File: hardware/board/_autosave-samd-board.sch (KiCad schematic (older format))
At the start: 26 parts, among them J1 USB_B_Mini, J2 Conn_ARM_JTAG_SWD_10, J3 Conn_01x16_Male, J4 Conn_01x16_Male, SW1 SW_Push, U1 AZ1117-3.3, U2 ATSAMD21E17D-A, Y1 8MHz

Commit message: increase pin count from 28 to 32, complete routing
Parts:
- C2: value 10u 10V -> 10u 16V
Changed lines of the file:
@@
 P 5700 1750
 F 0 "C2" H 5550 1800 50  0000 R CNN
-F 1 "10u 10V" H 5550 1700 50  0000 R CNN
+F 1 "10u 16V" H 5550 1700 50  0000 R CNN
 F 2 "Capacitor_Tantalum_SMD:CP_EIA-3216-18_Kemet-A_Pad1.58x1.35mm_HandSolder" H 5738 1600 50  0001 C CNN
 F 3 "~" H 5700 1750 50  0001 C CNN

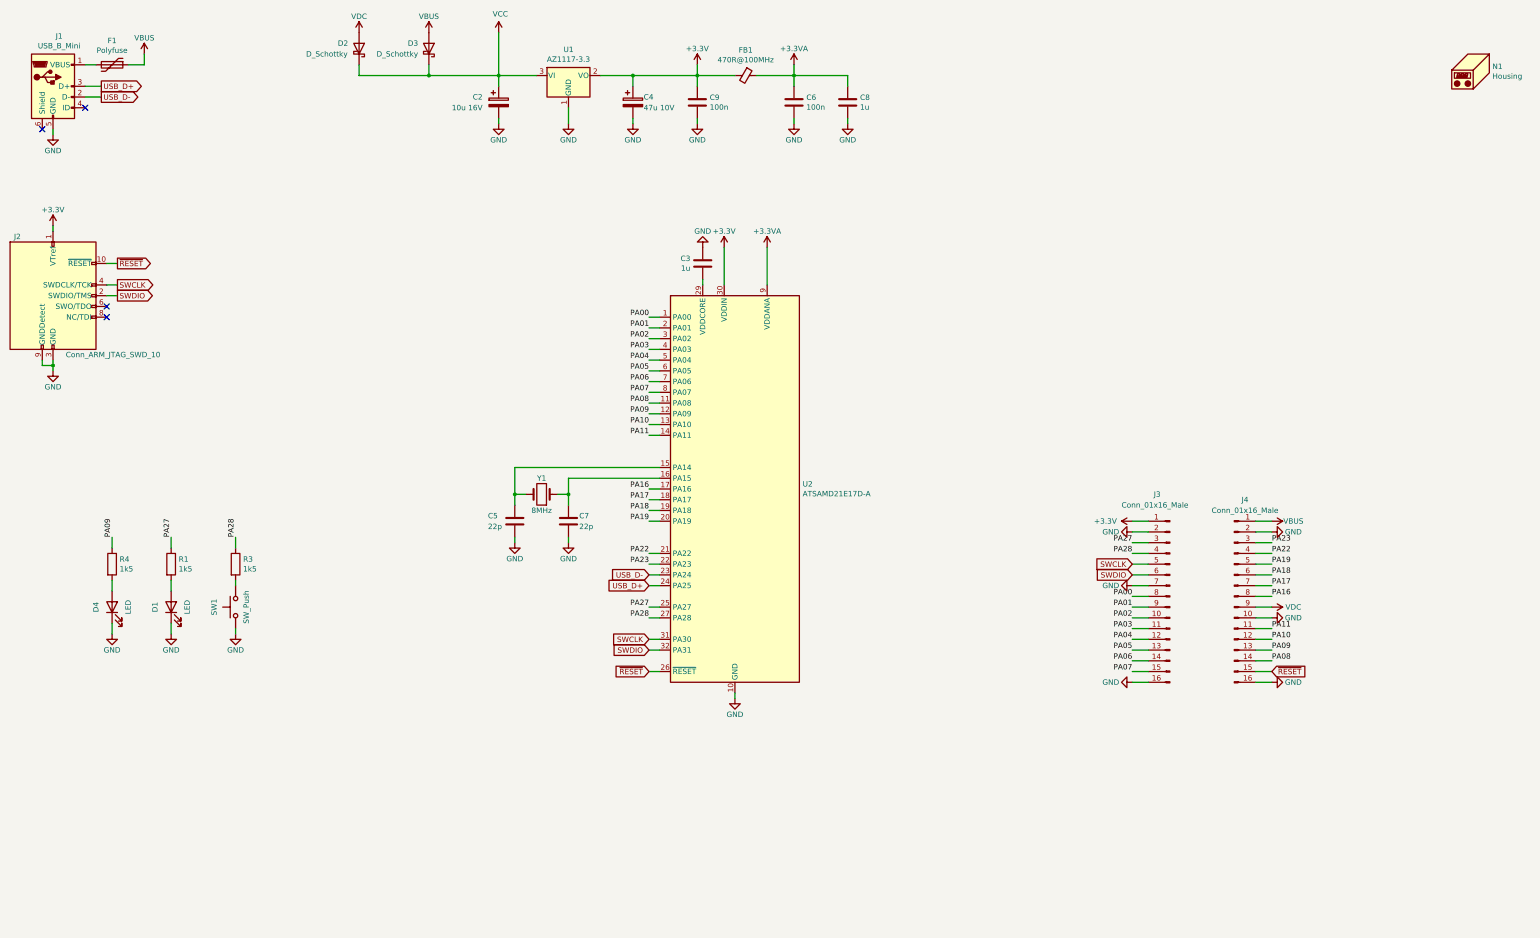
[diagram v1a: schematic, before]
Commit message: complete component silkscreen placement
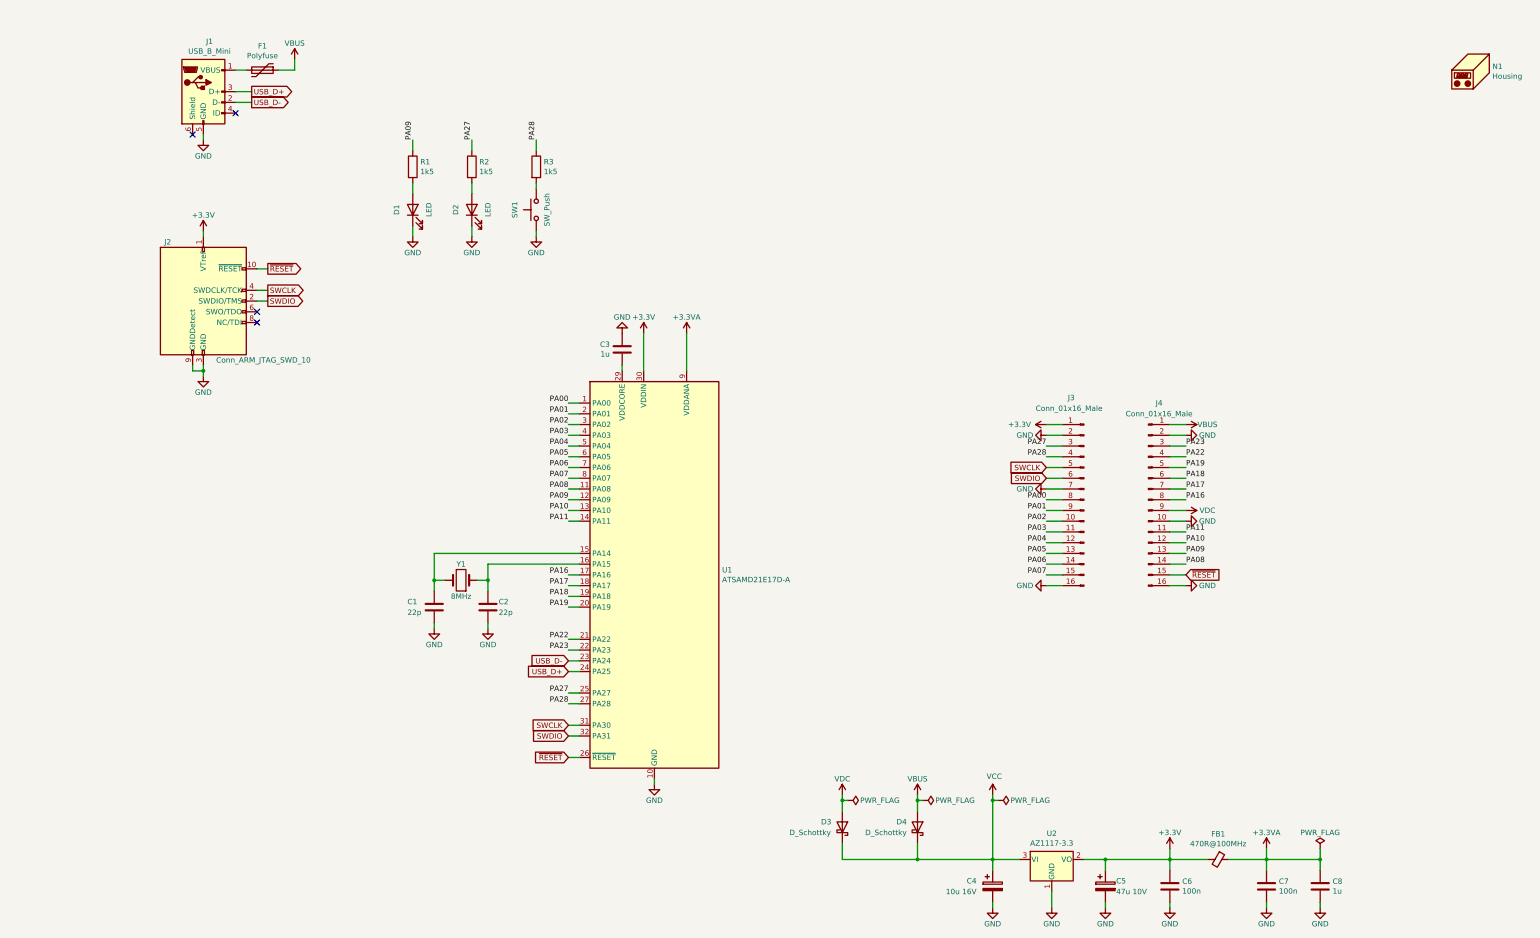
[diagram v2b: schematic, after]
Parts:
- renumbered C5 to C1, C7 to C2, C2 to C4, C4 to C5, C9 to C6, C6 to C7, D4 to D1, D1 to D2, D2 to D3, D3 to D4, R4 to R1, R1 to R2, U2 to U1, U1 to U2
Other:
- moved on the sheet: C1, C2, C3, C4, C5, C6, C7, C8, D1, D2, D3, D4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

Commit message: add power LED, pin silkscreen markers
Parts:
- added D5: LED, Assorted:LED_0603_1608Metric_Pad1.05x0.95mm_HandSolder, symbol Device:LED
- added R4: 1k5, Resistor_SMD:R_0603_1608Metric_Pad0.98x0.95mm_HandSolder, symbol Device:R
- D1, D2: footprint LED_SMD:LED_0603_1608Metric_Pad1.05x0.95mm_HandSolder -> Assorted:LED_0603_1608Metric_Pad1.05x0.95mm_HandSolder
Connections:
- net +3V3: now also R4.1
- net GND: now also D5.1 (K)
- new net: D5.2 (A), R4.2
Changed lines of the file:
@@
 U 1 1 60DF4799
 P 7150 6150
-F 0 "U1" H 7780 6196 50  0000 L CNN
-F 1 "ATSAMD21E17D-A" H 7780 6105 50  0000 L CNN
+F 0 "U1" H 7650 8000 50  0000 L CNN
+F 1 "ATSAMD21E17D-A" H 7300 4300 50  0000 L CNN
 F 2 "Package_QFP:TQFP-32_7x7mm_P0.8mm" H 8050 4300 50  0001 C CNN
 F 3 "http://ww1.microchip.com/downloads/en/DeviceDoc/SAM_D21_DA1_Family_Data%20Sheet_DS40001882E.pdf" H 7150 6150 50  0001 C CNN
@@
 F 0 "D2" H 5450 2900 50  0000 C CNN
 F 1 "LED" H 5450 2600 50  0000 C CNN
-F 2 "LED_SMD:LED_0603_1608Metric_Pad1.05x0.95mm_HandSolder" H 5450 2750 50  0001 C CNN
+F 2 "Assorted:LED_0603_1608Metric_Pad1.05x0.95mm_HandSolder" H 5450 2750 50  0001 C CNN
 F 3 "~" H 5450 2750 50  0001 C CNN
 	1    5450 2750
@@
 F 0 "D1" H 4900 2900 50  0000 C CNN
 F 1 "LED" H 4900 2600 50  0000 C CNN
-F 2 "LED_SMD:LED_0603_1608Metric_Pad1.05x0.95mm_HandSolder" H 4900 2750 50  0001 C CNN
+F 2 "Assorted:LED_0603_1608Metric_Pad1.05x0.95mm_HandSolder" H 4900 2750 50  0001 C CNN
 F 3 "~" H 4900 2750 50  0001 C CNN
 	1    4900 2750
@@
 	1    0    0    -1
 $EndComp
+$Comp
+L Device:LED D5
+U 1 1 60E95663
+P 7100 2750
+F 0 "D5" H 7100 2900 50  0000 C CNN
+F 1 "LED" H 7100 2600 50  0000 C CNN
+F 2 "Assorted:LED_0603_1608Metric_Pad1.05x0.95mm_HandSolder" H 7100 2750 50  0001 C CNN
+F 3 "~" H 7100 2750 50  0001 C CNN
+	1    7100 2750
+	0    -1   -1   0
+$EndComp
+$Comp
+L Device:R R4
+U 1 1 60E95681
+P 7100 2350
+F 0 "R4" H 7170 2396 50  0000 L CNN
+F 1 "1k5" H 7170 2305 50  0000 L CNN
+F 2 "Resistor_SMD:R_0603_1608Metric_Pad0.98x0.95mm_HandSolder" V 7030 2350 50  0001 C CNN
+F 3 "~" H 7100 2350 50  0001 C CNN
+	1    7100 2350
+	1    0    0    -1
+$EndComp
+Wire Wire Line
+	7100 2200 7100 2100
+Wire Wire Line
+	7100 2500 7100 2600
+Wire Wire Line
+	7100 2900 7100 3000
+$Comp
+L power:GND #PWR0101
+U 1 1 60E9568E
+P 7100 3000
+F 0 "#PWR0101" H 7100 2750 50  0001 C CNN
+F 1 "GND" H 7100 2850 50  0000 C CNN
+F 2 "" H 7100 3000 50  0001 C CNN
+F 3 "" H 7100 3000 50  0001 C CNN
+	1    7100 3000
+	1    0    0    -1
+$EndComp
+$Comp
+L power:+3.3V #PWR0102
+U 1 1 60E9FD37
+P 7100 2100
+F 0 "#PWR0102" H 7100 1950 50  0001 C CNN
+F 1 "+3.3V" H 7100 2250 50  0000 C CNN
+F 2 "" H 7100 2100 50  0001 C CNN
+F 3 "" H 7100 2100 50  0001 C CNN
+	1    7100 2100
+	1    0    0    -1
+$EndComp
